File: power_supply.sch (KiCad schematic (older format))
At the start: 40 parts, among them IC1 TPS54561DPRT, J2 PJ-202A, U1 TPS62823DLCT, U2 TPS62823DLCT

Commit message: Block diagram update
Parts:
- BAT1: footprint sc606-baseboard-footprints:BU1632SM -> antmicro-footprints:BU1632SM; symbol sc606-baseboard:BU1632SM -> antmicroBatteryHoldersClipsContacts:BU1632SM
- C17, C18, C19: footprint sc606-baseboard-footprints:0805-cap -> antmicro-footprints:0805-cap; symbol sc606-baseboard:C_2u2_0805_50V -> antmicroCapacitorsmisc:C_2u2_0805_50V
- C20: footprint sc606-baseboard-footprints:0402-cap -> antmicro-footprints:0402-cap; symbol sc606-baseboard:C_10n_0402 -> antmicroCapacitors0402:C_10n_0402
- C21: footprint sc606-baseboard-footprints:0402-cap -> antmicro-footprints:0402-cap; symbol sc606-baseboard:C_4n7_0402 -> antmicroCapacitors0402:C_4n7_0402
- C22: footprint sc606-baseboard-footprints:0402-cap -> antmicro-footprints:0402-cap; symbol sc606-baseboard:C_47p_0402 -> antmicroCapacitors0402:C_47p_0402
- C23: footprint sc606-baseboard-footprints:0402-cap -> antmicro-footprints:0402-cap; symbol sc606-baseboard:C_100n_0402 -> antmicroCapacitors0402:C_100n_0402
- C24, C25, C26: footprint sc606-baseboard-footprints:0603-cap -> antmicro-footprints:0603-cap; symbol sc606-baseboard:C_47u_0603 -> antmicroCapacitors0603:C_47u_0603
- C27, C28: footprint sc606-baseboard-footprints:0402-cap -> antmicro-footprints:0402-cap; symbol sc606-baseboard:C_2u2_0402 -> antmicroCapacitors0402:C_2u2_0402
- C29, C30: footprint sc606-baseboard-footprints:0603-cap -> antmicro-footprints:0603-cap; symbol sc606-baseboard:C_100p_0603 -> antmicroCapacitors0603:C_100p_0603
- C31, C32: footprint sc606-baseboard-footprints:0402-cap -> antmicro-footprints:0402-cap; symbol sc606-baseboard:C_10u_0402 -> antmicroCapacitors0402:C_10u_0402
- D3, D4: footprint sc606-baseboard-footprints:TO-277A -> face-scanner-led-board-footprints:TO-277A; symbol sc606-baseboard:V8PM45-M3_H -> antmicroDiodesRectifiersSingle:V8PM45-M3_H
- D?1: footprint sc606-baseboard-footprints:PDS760-13 -> antmicro-footprints:PDS760-13; symbol sc606-baseboard:PDS760-13 -> antmicroDiodesRectifiersSingle:PDS760-13
- IC1: footprint sc606-baseboard-footprints:WSON-10_4x4 -> antmicro-footprints:WSON-10_4x4; symbol sc606-baseboard:TPS54561DPRT -> antmicroPMICVoltageRegulatorsLinear:TPS54561DPRT
- J2: footprint sc606-baseboard-footprints:Barrel_Jack_5.5mmODx2.1mmID_PJ-202A -> antmicro-footprints:Barrel_Jack_5.5mmODx2.1mmID_PJ-202A; symbol sc606-baseboard:PJ-202A -> antmicroBarrelPowerConnectors:PJ-202A
- L1: footprint sc606-baseboard-footprints:WE_7447798720 -> antmicro-footprints:WE_7447798720; symbol sc606-baseboard:7447798720 -> antmicroFixedInductors:7447798720
- L2, L3: footprint sc606-baseboard-footprints:IHLP-1212AE -> antmicro-footprints:IHLP-1212AE; symbol sc606-baseboard:IHLP1212AEERR47M11 -> antmicroFixedInductors:IHLP1212AEERR47M11
- R10, R11, R4: footprint sc606-baseboard-footprints:0402-res -> antmicro-footprints:0402-res; symbol sc606-baseboard:R_10k_0402 -> antmicroResistors0402:R_10k_0402
- R12, R14, R3: footprint sc606-baseboard-footprints:0402-res -> antmicro-footprints:0402-res; symbol sc606-baseboard:R_243k_0402 -> antmicroResistors0402:R_243k_0402
- R13, R15, R8: footprint sc606-baseboard-footprints:0402-res -> antmicro-footprints:0402-res; symbol sc606-baseboard:R_53k6_0402 -> antmicroResistors0402:R_53k6_0402
- R5: footprint sc606-baseboard-footprints:0402-res -> antmicro-footprints:0402-res; symbol sc606-baseboard:R_16k9_0402 -> antmicroResistors0402:R_16k9_0402
- R6: footprint sc606-baseboard-footprints:0402-res -> antmicro-footprints:0402-res; symbol sc606-baseboard:R_100k_0402 -> antmicroResistors0402:R_100k_0402
- R7: footprint sc606-baseboard-footprints:0603-res -> antmicro-footprints:0603-res; symbol sc606-baseboard:R_49R9_0603 -> antmicroResistors0603:R_49R9_0603
- R9: footprint sc606-baseboard-footprints:0402-res -> antmicro-footprints:0402-res; symbol sc606-baseboard:R_10k2_0402 -> antmicroResistors0402:R_10k2_0402
- U1, U2: footprint sc606-baseboard-footprints:QFN-8_2x1mm -> antmicro-footprints:QFN-8_2x1mm; symbol sc606-baseboard:TPS62823DLCT -> antmicroDCDCConverters:TPS62823DLCT

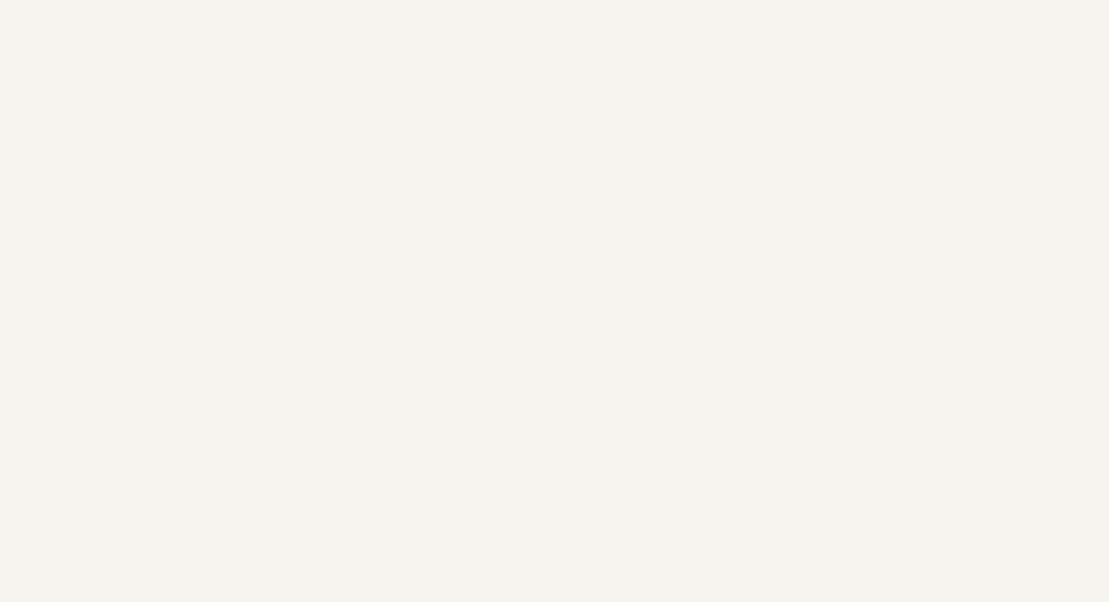
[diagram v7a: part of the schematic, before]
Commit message: Added connectors to LCD displays
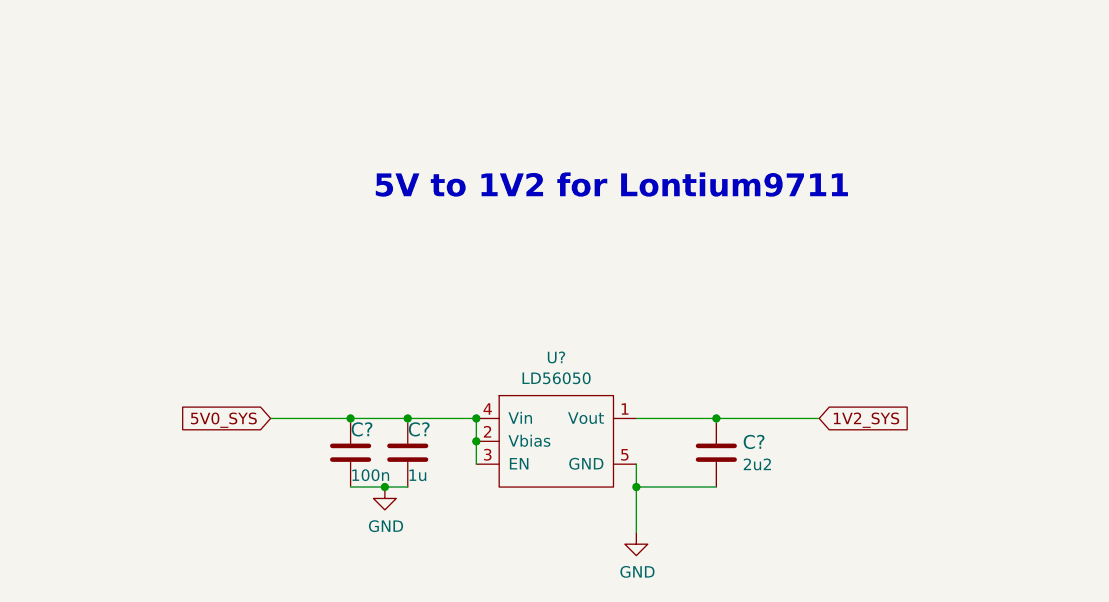
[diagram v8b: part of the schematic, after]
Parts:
- added C?: C_1u_0402, antmicro-footprints:0402-cap, symbol antmicroCapacitors0402:C_1u_0402
- added C?: C_100n_0402, antmicro-footprints:0402-cap, symbol antmicroCapacitors0402:C_100n_0402
- added C?: C_2u2_0402, antmicro-footprints:0402-cap, symbol antmicroCapacitors0402:C_2u2_0402
- added U?: LD56050, antmicro-footprints:DFN-4_1.2x1.2mm, symbol antmicroPMICVoltageRegulatorsLinear:LD56050
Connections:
- net 5V0_SYS: now also C?.1, C?.1, U?.2 (Vbias), U?.3 (EN), U?.4 (Vin)
- net GND: now also C?.2, C?.2, C?.2, U?.5 (GND)
- new net 1V2_SYS: C?.1, U?.1 (Vout)
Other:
- note added: "5V to 1V2 for Lontium9711\n"
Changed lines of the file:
@@
 Wire Wire Line
 	2600 5650 2150 5650
+Text Notes 2200 8300 0    100  ~ 20
+5V to 1V2 for Lontium9711\n
+$Comp
+L antmicroPMICVoltageRegulatorsLinear:LD56050 U?
+U 1 1 6203CFC7
+P 3000 9350
+F 0 "U?" H 3000 9715 50  0000 C CNN
+F 1 "LD56050" H 3000 9624 50  0000 C CNN
+F 2 "antmicro-footprints:DFN-4_1.2x1.2mm" H 3100 9500 50  0001 C CNN
+F 3 "https://www.mouser.pl/datasheet/2/389/dm00472468-1799145.pdf" H 3100 9500 50  0001 C CNN
+F 4 "STMicroelectronics" H 3100 9100 50  0001 C CNN "Manufacturer"
+F 5 "LD56050DPU120R" H 3100 9000 50  0001 C CNN "MPN"
+	1    3000 9350
+	1    0    0    -1
+$EndComp
+$Comp
+L power:GND #PWR?
+U 1 1 6203DC2F
+P 3350 9750
+F 0 "#PWR?" H 3350 9500 50  0001 C CNN
+F 1 "GND" H 3355 9577 50  0000 C CNN
+F 2 "" H 3350 9750 50  0001 C CNN
+F 3 "" H 3350 9750 50  0001 C CNN
+	1    3350 9750
+	1    0    0    -1
+$EndComp
+Wire Wire Line
+	3350 9450 3350 9550
+Text GLabel 1750 9250 0    50   Input ~ 0
+5V0_SYS
+Wire Wire Line
+	1750 9250 2100 9250
+Wire Wire Line
+	2650 9450 2650 9350
+Connection ~ 2650 9250
+Connection ~ 2650 9350
+Wire Wire Line
+	2650 9350 2650 9250
+$Comp
+L antmicroCapacitors0402:C_1u_0402 C?
+U 1 1 620460ED
+P 2350 9400
+F 0 "C?" H 2350 9500 60  0000 L CNN
+F 1 "C_1u_0402" H 2350 9250 60  0001 C CNN
+F 2 "antmicro-footprints:0402-cap" H 2550 9600 60  0001 L CNN
+F 3 "" H 2350 9400 50  0001 C CNN
+F 4 "TDK" H 2550 9800 60  0001 L CNN "Manufacturer"
+F 5 "C1005X6S1A105K050BC" H 2550 9700 60  0001 L CNN "MPN"
+F 6 "1u" H 2350 9300 50  0000 L CNN "Val"
+	1    2350 9400
+	1    0    0    -1
+$EndComp
+Connection ~ 2350 9250
+Wire Wire Line
+	2350 9250 2650 9250
+$Comp
+L antmicroCapacitors0402:C_100n_0402 C?
+U 1 1 6204728D
+P 2100 9400
+F 0 "C?" H 2100 9500 60  0000 L CNN
+F 1 "C_100n_0402" H 2100 9250 60  0001 C CNN
+F 2 "antmicro-footprints:0402-cap" H 2300 9600 60  0001 L CNN
+F 3 "" H 2100 9400 50  0001 C CNN
+F 4 "Murata" H 2300 9800 60  0001 L CNN "Manufacturer"
+F 5 "GRM155R61H104KE14D" H 2300 9700 60  0001 L CNN "MPN"
+F 6 "100n" H 2100 9300 50  0000 L CNN "Val"
+	1    2100 9400
+	1    0    0    -1
+$EndComp
+Connection ~ 2100 9250
+Wire Wire Line
+	2100 9250 2350 9250
+$Comp
+L antmicroCapacitors0402:C_2u2_0402 C?
+U 1 1 62047E87
+P 3700 9400
+F 0 "C?" H 3815 9445 60  0000 L CNN
+F 1 "C_2u2_0402" H 3700 9250 60  0001 C CNN
+F 2 "antmicro-footprints:0402-cap" H 3900 9600 60  0001 L CNN
+F 3 "" H 3700 9400 50  0001 C CNN
+F 4 "TDK" H 3900 9800 60  0001 L CNN "Manufacturer"
+F 5 "C1005X5R1A225K050BC" H 3900 9700 60  0001 L CNN "MPN"
+F 6 "2u2" H 3815 9347 50  0000 L CNN "Val"
+	1    3700 9400
+	1    0    0    -1
+$EndComp
+Wire Wire Line
+	3700 9550 3350 9550
+Connection ~ 3350 9550
+Wire Wire Line
+	3350 9550 3350 9750
+Wire Wire Line
+	2350 9550 2250 9550
+$Comp
+L power:GND #PWR?
+U 1 1 6204D9DB
+P 2250 9550
+F 0 "#PWR?" H 2250 9300 50  0001 C CNN
+F 1 "GND" H 2255 9377 50  0000 C CNN
+F 2 "" H 2250 9550 50  0001 C CNN
+F 3 "" H 2250 9550 50  0001 C CNN
+	1    2250 9550
+	1    0    0    -1
+$EndComp
+Connection ~ 2250 9550
+Wire Wire Line
+	2250 9550 2100 9550
+Wire Wire Line
+	3350 9250 3700 9250
+Connection ~ 3700 9250
+Wire Wire Line
+	3700 9250 4150 9250
+Text GLabel 4150 9250 2    50   Input ~ 0
+1V2_SYS
 $EndSCHEMATC
